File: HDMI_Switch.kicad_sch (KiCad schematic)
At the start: 1 part, among them U4 HD3SS215RTQR

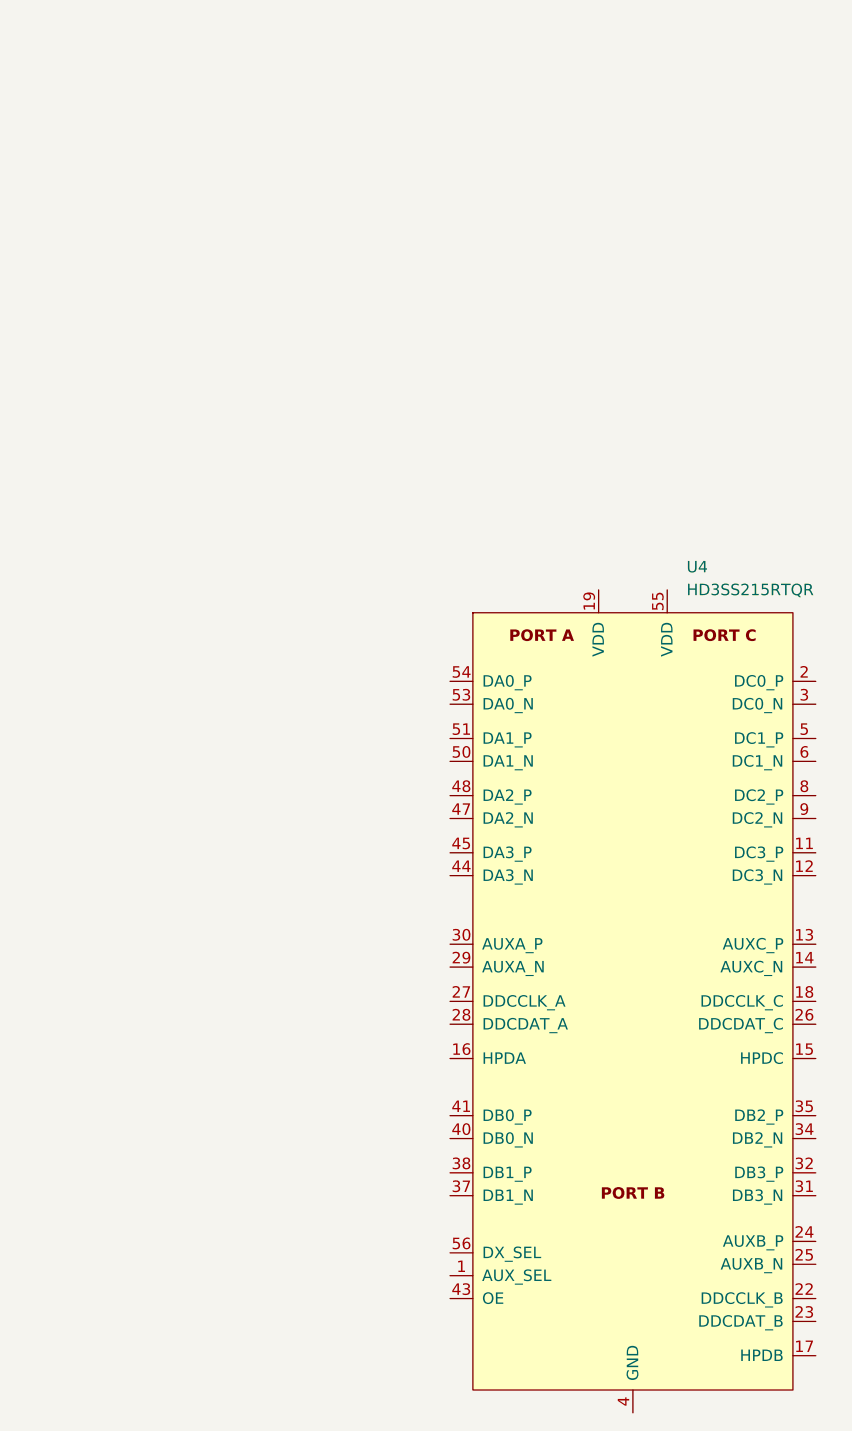
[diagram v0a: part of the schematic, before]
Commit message: Updated symbols' DigiKey part no.
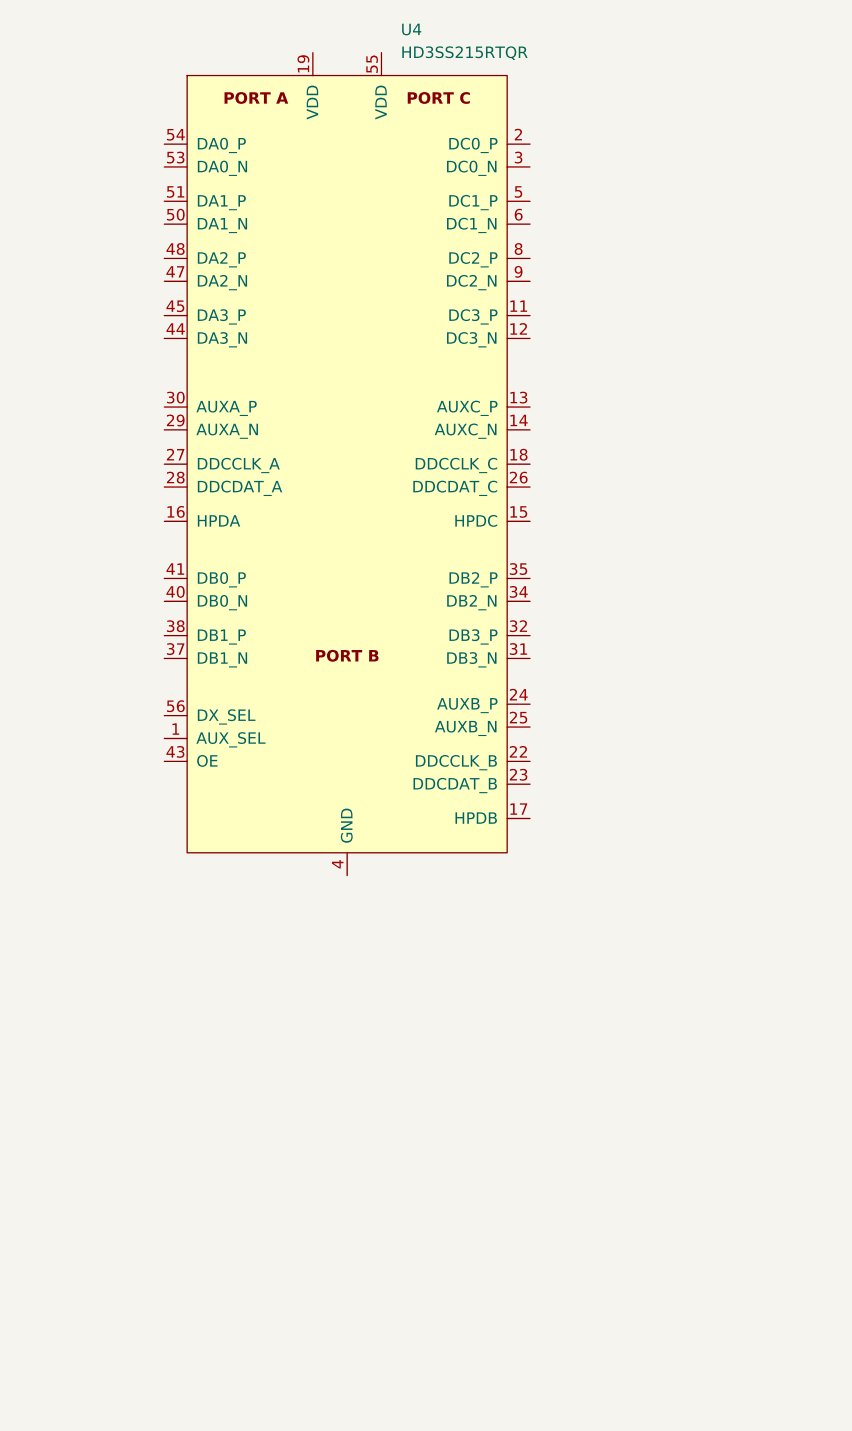
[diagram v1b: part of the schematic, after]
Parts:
- U4: DigiKey (none) -> 296-42335-1-ND
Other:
- moved on the sheet: U4
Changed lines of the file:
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@@
 	(symbol
 		(lib_id "HD3SS215RTQR:HD3SS215RTQR")
-		(at 223.52 146.05 0)
+		(at 191.77 86.36 0)
 		(unit 1)
 		(body_style 1)
@@
 		(fields_autoplaced yes)
 		(property "Reference" "U4"
-			(at 229.4733 109.22 0)
+			(at 197.7233 49.53 0)
 			(show_name no)
 			(do_not_autoplace no)
@@
 		)
 		(property "Value" "HD3SS215RTQR"
-			(at 229.4733 111.76 0)
+			(at 197.7233 52.07 0)
 			(show_name no)
 			(do_not_autoplace no)
@@
 		)
 		(property "Footprint" "Package_DFN_QFN:QFN-56-1EP_8x8mm_P0.5mm_EP4.3x4.3mm"
-			(at 223.52 146.05 0)
+			(at 191.77 86.36 0)
 			(hide yes)
 			(show_name no)
@@
 		)
 		(property "Datasheet" "https://www.ti.com/lit/ds/symlink/hd3ss215.pdf"
-			(at 223.52 146.05 0)
+			(at 191.77 86.36 0)
 			(hide yes)
 			(show_name no)
@@
 		)
 		(property "Description" "6-Gbps HDMI / DisplayPort 2:1 / 1:2 differential switch, 56-pin RTQ VQFN"
-			(at 223.52 146.05 0)
+			(at 191.77 86.36 0)
 			(hide yes)
 			(show_name no)
+			(do_not_autoplace no)
+			(effects
+				(font
+					(size 1.27 1.27)
+				)
+			)
+		)
+		(property "DigiKey" "296-42335-1-ND"
+			(at 191.77 86.36 0)
+			(hide yes)
+			(show_name no)

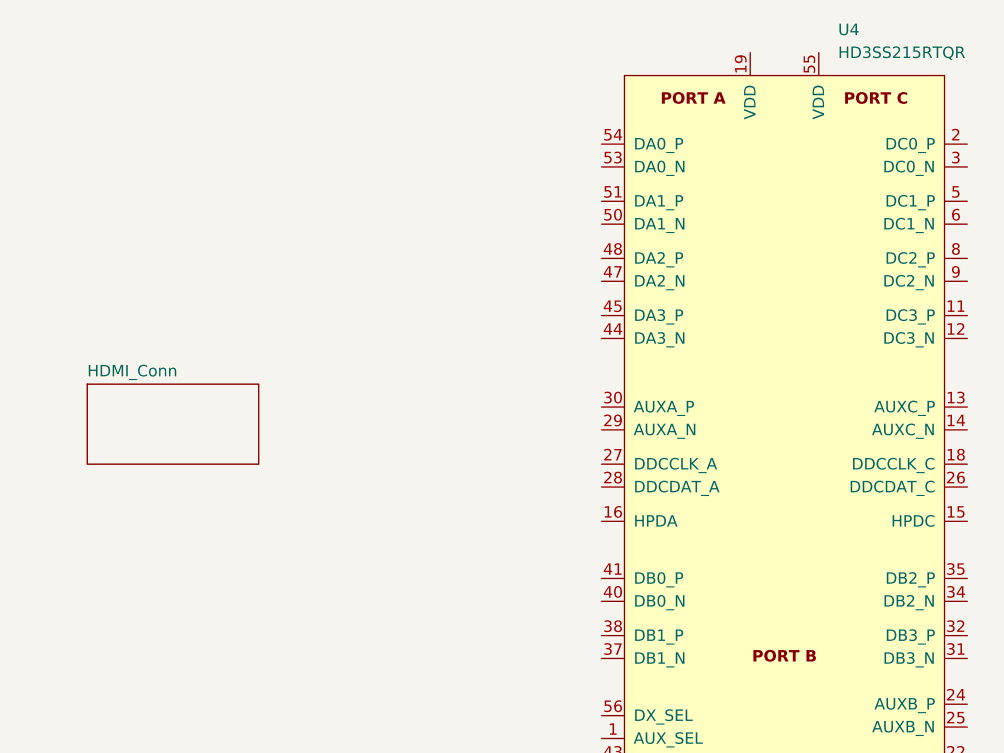
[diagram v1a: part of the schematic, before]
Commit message: Changed MCU & Stared routing HDMI connectiors
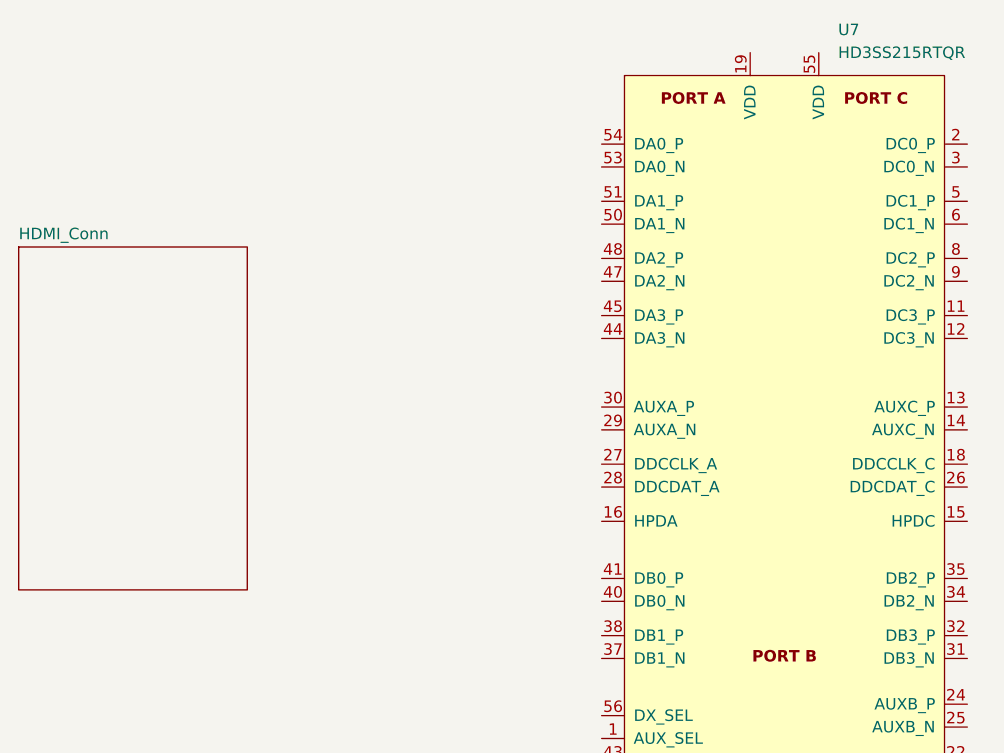
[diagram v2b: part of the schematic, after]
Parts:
- renumbered U4 to U7
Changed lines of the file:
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@@
 		(dnp no)
 		(fields_autoplaced yes)
-		(property "Reference" "U4"
+		(property "Reference" "U7"
 			(at 197.7233 49.53 0)
 			(show_name no)
@@
 			(project "KVM_Switch"
 				(path "/94386106-ccd4-487f-b5c5-d52ec3dd59db/6e43926c-16e0-4a92-a7fc-ce5a89c8ce59"
-					(reference "U4")
+					(reference "U7")
 					(unit 1)
 				)
@@
 	)
 	(sheet
-		(at 114.3 88.9)
-		(size 19.05 8.89)
+		(at 106.68 73.66)
+		(size 25.4 38.1)
 		(exclude_from_sim no)
 		(in_bom yes)
@@
 		)
 		(fill
-			(color 0 0 0 0)
+			(color 255 255 194 1)
 		)
 		(property "Sheetname" "HDMI_Conn"
-			(at 114.3 88.1884 0)
+			(at 106.68 72.9484 0)
 			(show_name no)
 			(do_not_autoplace no)
@@
 		)
 		(property "Sheetfile" "HDMI_Conn.kicad_sch"
-			(at 114.3 98.3746 0)
-			(hide yes)
-			(show_name no)
+			(at 106.68 112.3446 0)
+			(hide yes)
+			(show_name no)

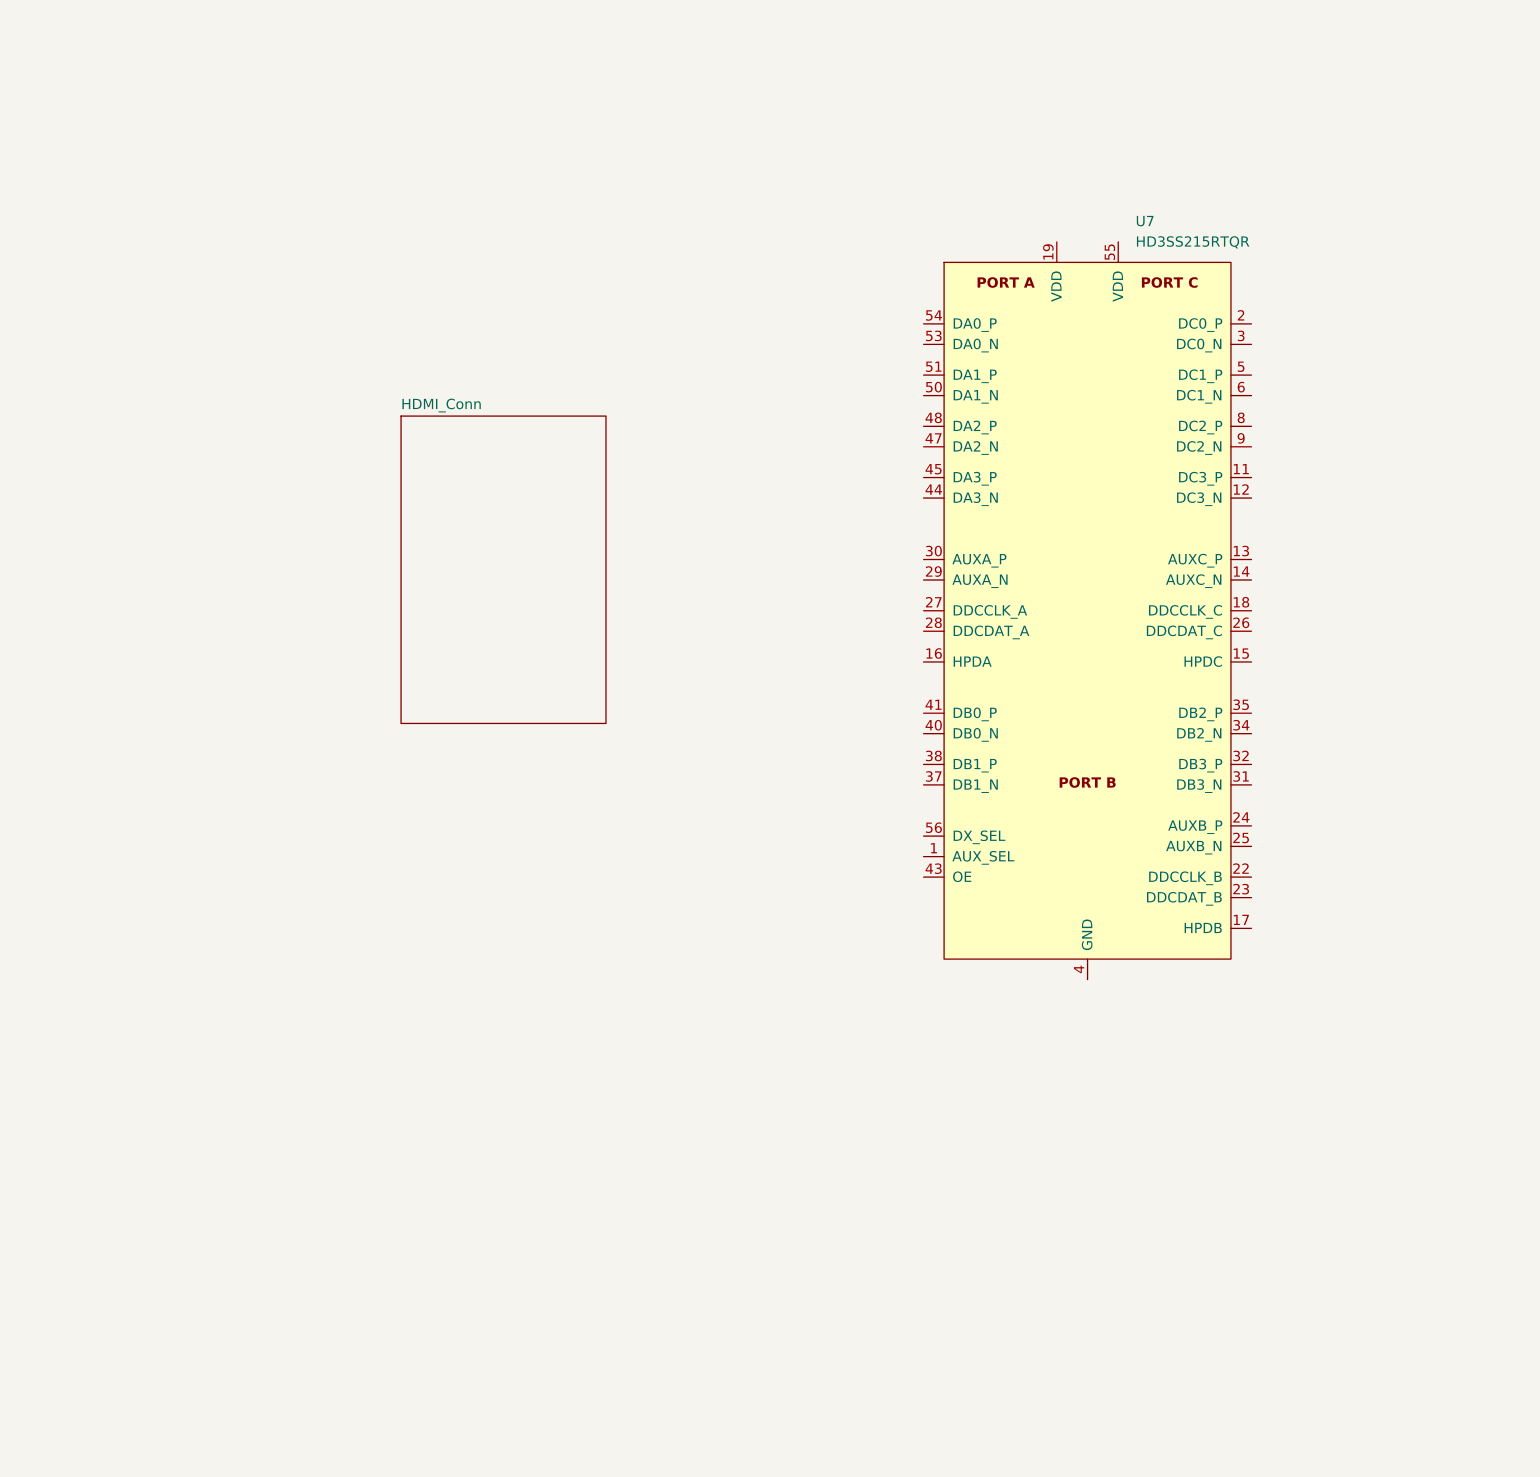
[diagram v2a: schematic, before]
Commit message: HDMI schematics
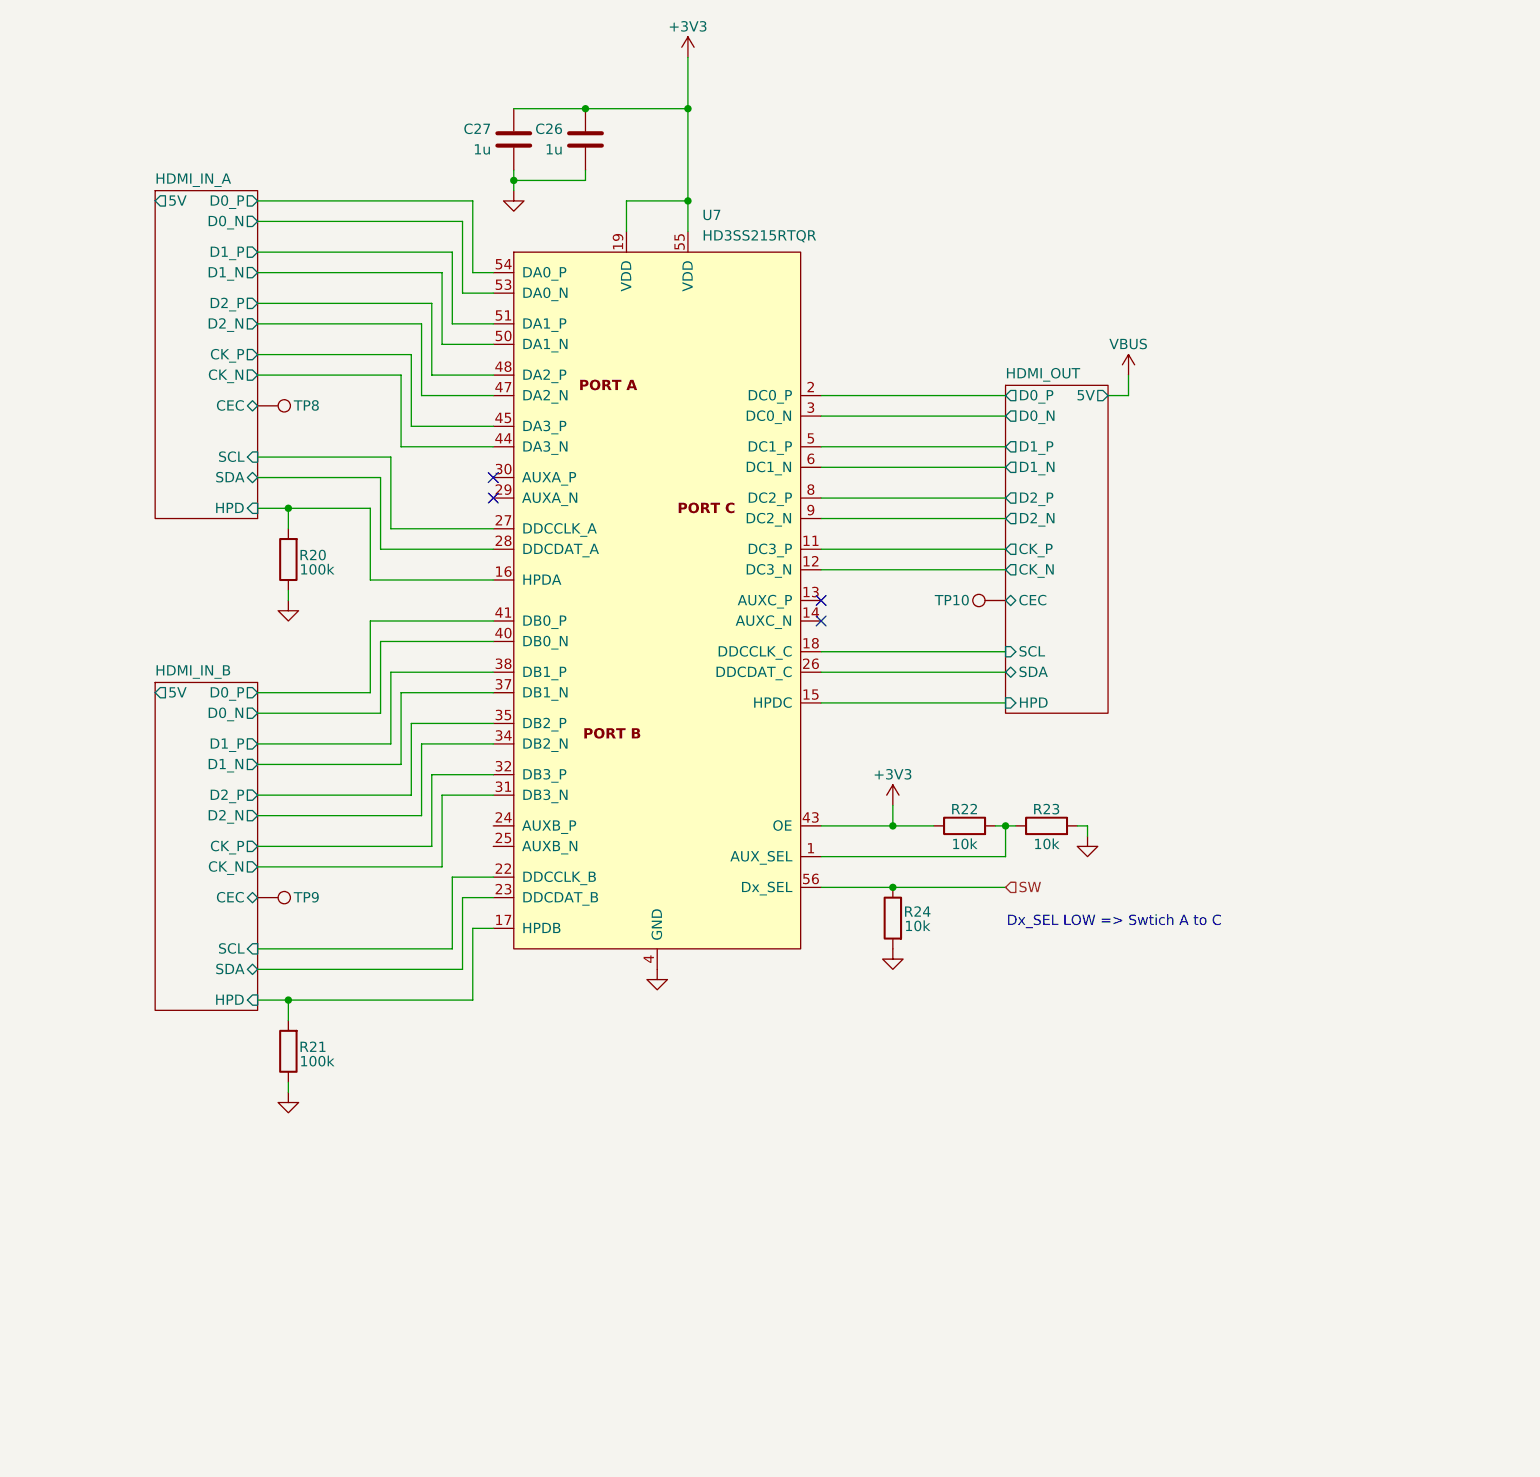
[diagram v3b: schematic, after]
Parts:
- added C26, C27: 1u, Capacitor_SMD:C_0402_1005Metric, symbol Device:C
- added R20, R21: 100k, Resistor_SMD:R_0603_1608Metric, symbol Device:R
- added R22, R23, R24: 10k, Resistor_SMD:R_0402_1005Metric, symbol Device:R
- added TP10, TP8, TP9: TestPoint, TestPoint:TestPoint_Pad_D1.0mm, symbol Connector:TestPoint
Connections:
- net GND: now also U7.4 (GND), C26.2, C27.2, R20.1, R21.1, R23.2, R24.2
- net at U7.1 (AUX_SEL): now also R22.2, R23.1
- net HDMI_OUT/CK_P: now reaches U7.11 (DC3_P)
- net HDMI_OUT/CK_N: now reaches U7.12 (DC3_N)
- net HDMI_OUT/HPD: now reaches U7.15 (HPDC)
- net HDMI_IN_A/HPD: now reaches U7.16 (HPDA)
- net HDMI_IN_A/HPD: now also R20.2
- net HDMI_IN_B/HPD: now reaches U7.17 (HPDB)
- net HDMI_IN_B/HPD: now also R21.2
- net HDMI_OUT/SCL: now reaches U7.18 (DDCCLK_C)
- net +3V3: now reaches U7.19 (VDD)
- net +3V3: now also U7.43 (OE), U7.55 (VDD), C26.1, C27.1, R22.1
- net HDMI_OUT/D0_P: now reaches U7.2 (DC0_P)
- net HDMI_IN_B/SCL: now reaches U7.22 (DDCCLK_B)
- net HDMI_IN_B/SDA: now reaches U7.23 (DDCDAT_B)
- net HDMI_OUT/SDA: now reaches U7.26 (DDCDAT_C)
- net HDMI_IN_A/SCL: now reaches U7.27 (DDCCLK_A)
- net HDMI_IN_A/SDA: now reaches U7.28 (DDCDAT_A)
- net HDMI_OUT/D0_N: now reaches U7.3 (DC0_N)
- net HDMI_IN_B/CK_N: now reaches U7.31 (DB3_N)
- net HDMI_IN_B/CK_P: now reaches U7.32 (DB3_P)
- net HDMI_IN_B/D2_N: now reaches U7.34 (DB2_N)
- net HDMI_IN_B/D2_P: now reaches U7.35 (DB2_P)
- net HDMI_IN_B/D1_N: now reaches U7.37 (DB1_N)
- net HDMI_IN_B/D1_P: now reaches U7.38 (DB1_P)
- net HDMI_IN_B/D0_N: now reaches U7.40 (DB0_N)
- net HDMI_IN_B/D0_P: now reaches U7.41 (DB0_P)
- net HDMI_IN_A/CK_N: now reaches U7.44 (DA3_N)
- net HDMI_IN_A/CK_P: now reaches U7.45 (DA3_P)
- net HDMI_IN_A/D2_N: now reaches U7.47 (DA2_N)
- net HDMI_IN_A/D2_P: now reaches U7.48 (DA2_P)
- net HDMI_OUT/D1_P: now reaches U7.5 (DC1_P)
- net HDMI_IN_A/D1_N: now reaches U7.50 (DA1_N)
- net HDMI_IN_A/D1_P: now reaches U7.51 (DA1_P)
- net HDMI_IN_A/D0_N: now reaches U7.53 (DA0_N)
- net HDMI_IN_A/D0_P: now reaches U7.54 (DA0_P)
- net SW: now reaches U7.56 (Dx_SEL)
- net SW: now also R24.1
- net HDMI_OUT/D1_N: now reaches U7.6 (DC1_N)
- net HDMI_OUT/D2_P: now reaches U7.8 (DC2_P)
- net HDMI_OUT/D2_N: now reaches U7.9 (DC2_N)
- new net HDMI_IN_A/CEC: TP8.1
- new net HDMI_IN_B/CEC: TP9.1
- new net HDMI_OUT/CEC: TP10.1
- no-connect marks 0 -> 4
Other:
- sheet HDMI_Conn renamed HDMI_IN_A
- added sheet HDMI_IN_B (HDMI_IN.kicad_sch)
- added sheet HDMI_OUT (HDMI_OUT.kicad_sch)
- sheet HDMI_IN_A: file HDMI_Conn.kicad_sch -> HDMI_IN.kicad_sch
- sheet HDMI_IN_A ports: added 5V, CEC, CK_N, CK_P, D0_N, D0_P, D1_N, D1_P, D2_N, D2_P, HPD, SCL, SDA; removed none
- note added: "Dx_SEL LOW => Swtich A to C"
- moved on the sheet: U7

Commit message: Schematics done
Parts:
- added C29: 1u, Capacitor_SMD:C_0402_1005Metric, symbol Device:C
- added R25, R26: 47k, Resistor_SMD:R_0402_1005Metric, symbol Device:R
- added TP11, TP12: TestPoint, TestPoint:TestPoint_Pad_D1.0mm, symbol Connector:TestPoint
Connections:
- net GND: now also C29.2
- net HDMI_OUT/SCL: now also R25.1
- net HDMI_OUT/SDA: now also R26.1
- net VBUS: now also C29.1, R25.2, R26.2
- new net DET_A: TP12.1
- new net DET_B: TP11.1
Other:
- moved on the sheet: C26, C27
